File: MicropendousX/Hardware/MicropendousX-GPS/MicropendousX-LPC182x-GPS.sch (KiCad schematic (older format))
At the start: 0 parts

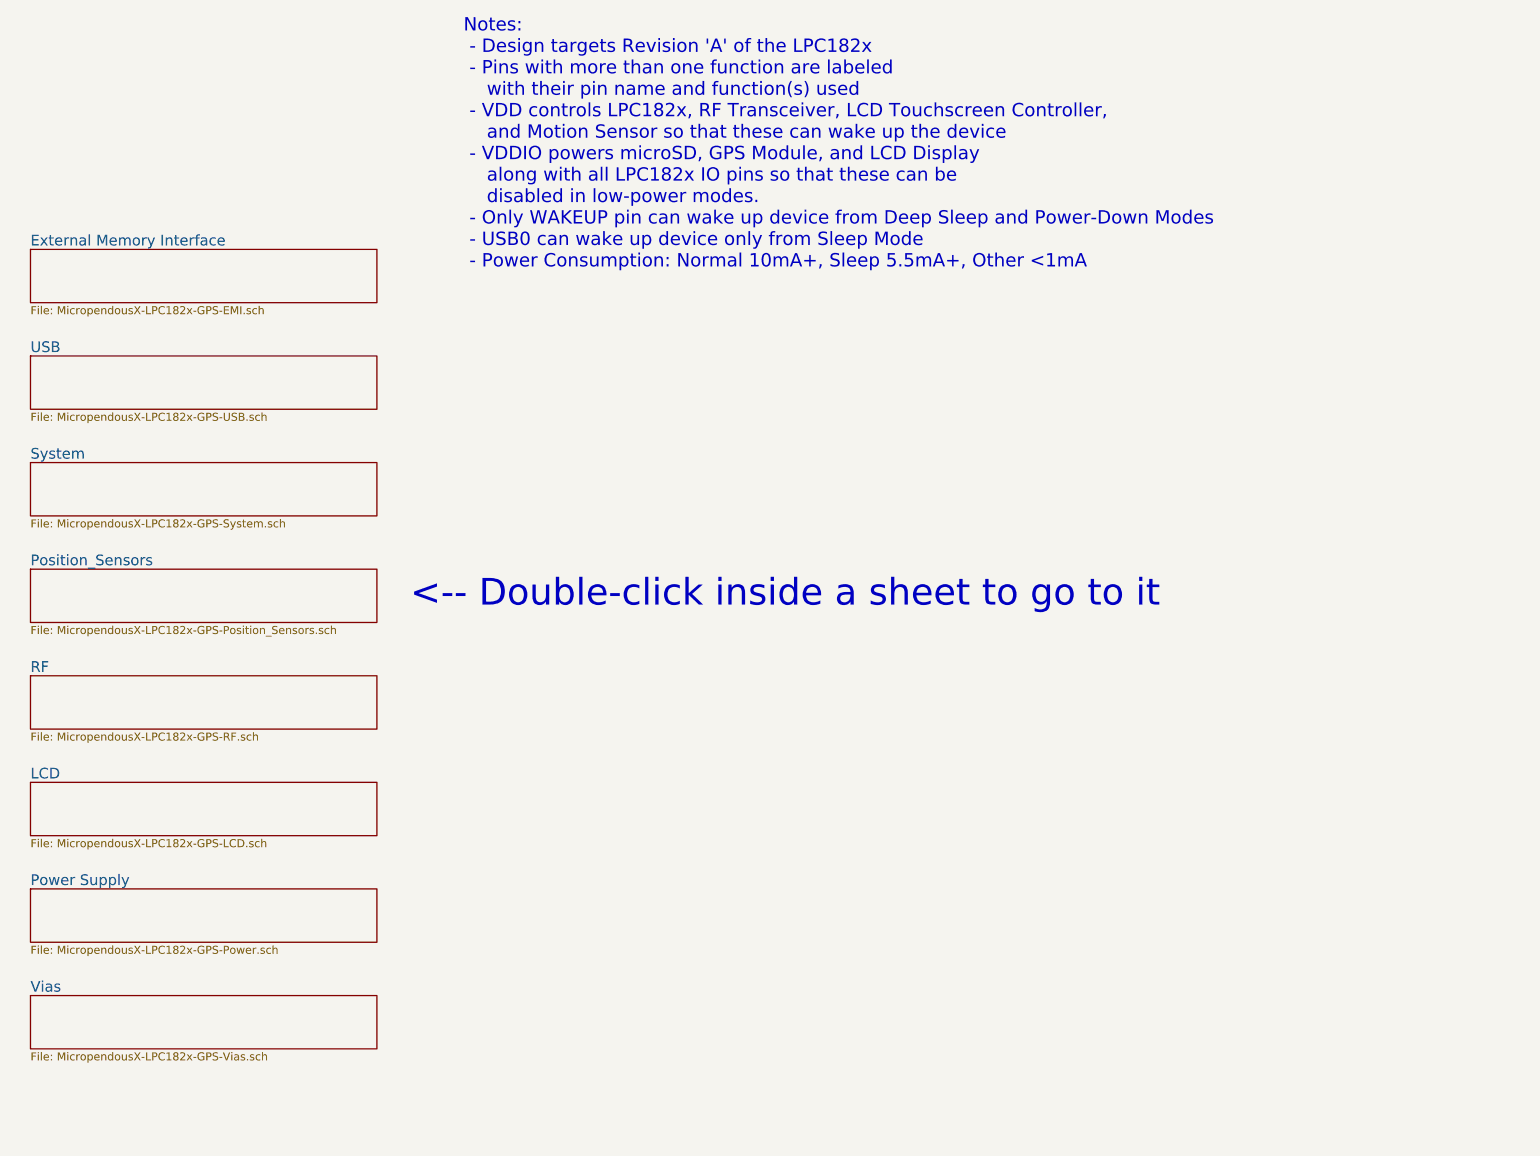
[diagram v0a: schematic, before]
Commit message: Updated MicropendousX-LPC182x-GPS design.  PCB routing almost complete.
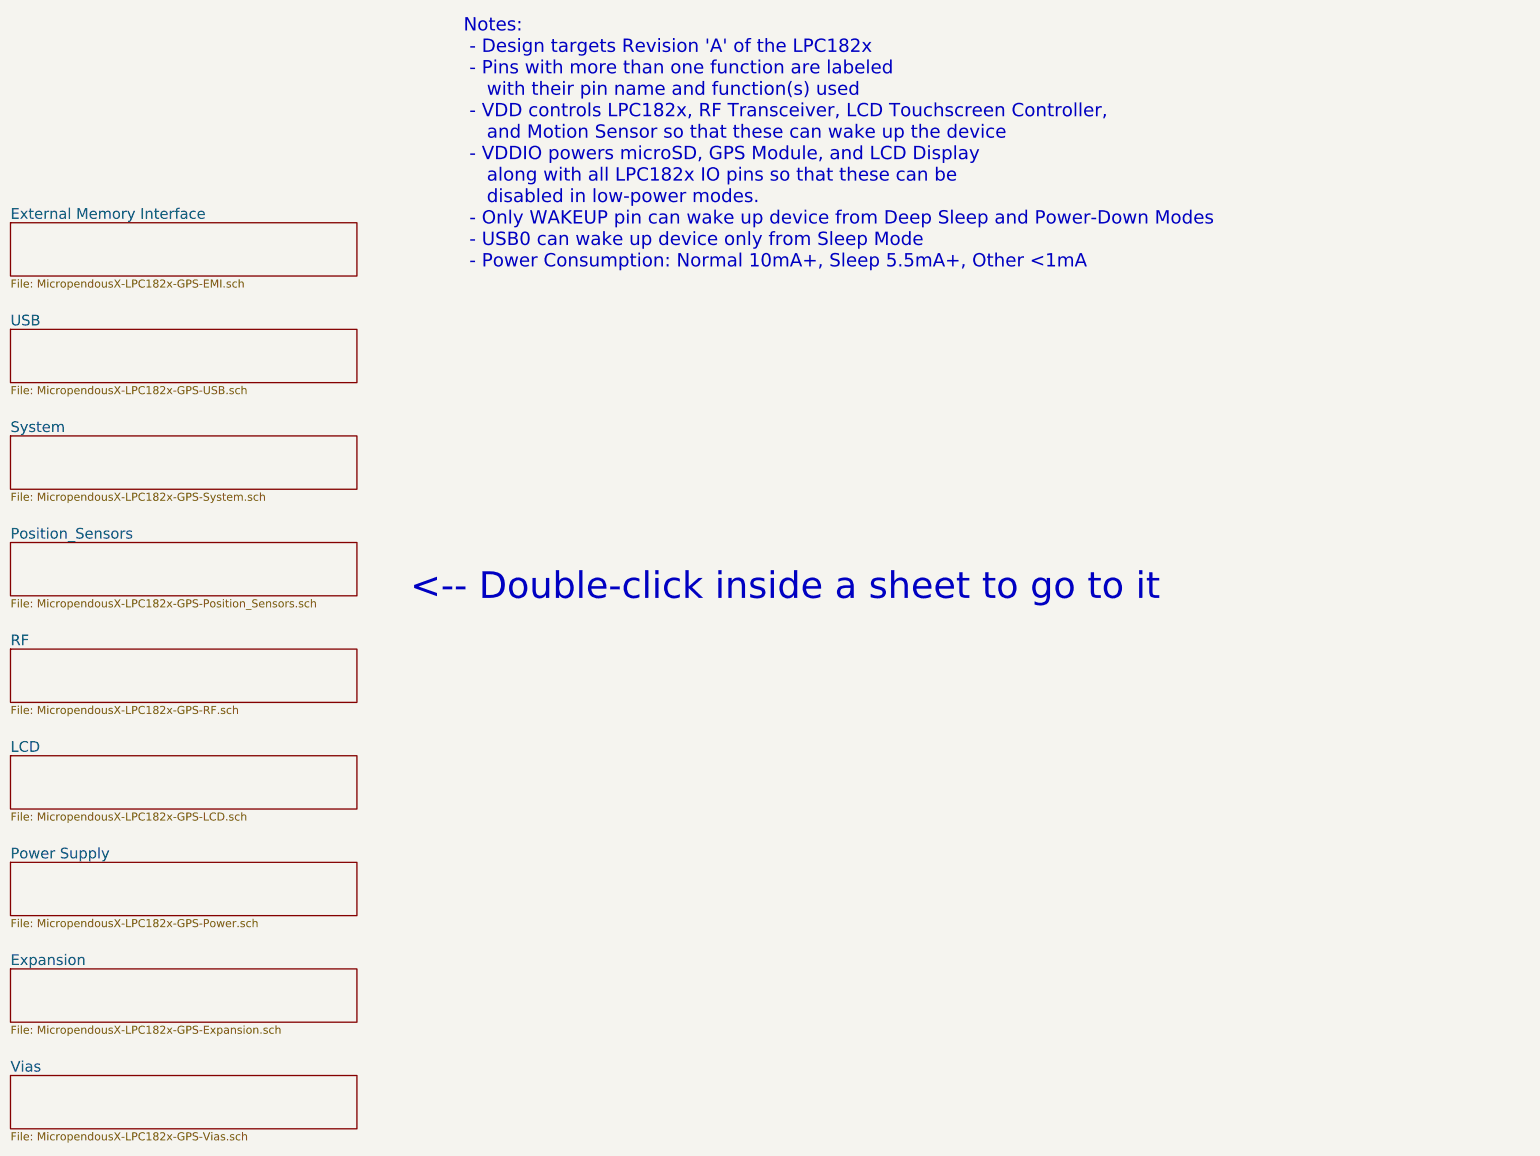
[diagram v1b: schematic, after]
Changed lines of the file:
@@
-EESchema Schematic File Version 2  date 5/31/2012 10:34:44 PM
+EESchema Schematic File Version 2  date 6/8/2012 3:21:19 PM
 LIBS:power
 LIBS:device
@@
 LIBS:contrib
 LIBS:valves
-LIBS:opendous
-LIBS:Opennect_Schematic_Symbols_Library
 LIBS:MicropendousX-LPC182x-GPS-cache
 EELAYER 25  0
@@
 $Descr A4 11700 8267
 encoding utf-8
-Sheet 1 9
+Sheet 1 10
 Title "MicropendousX-LPC182x-GPS"
-Date "1 jun 2012"
+Date "8 jun 2012"
 Rev "1.0"
 Comp "Opendous Inc."
@@
 $EndDescr
 $Sheet
-S 950  3400 2600 400
+S 800  7200 2600 400
+U 4FC9D4A0
+F0 "Vias" 80
+F1 "MicropendousX-LPC182x-GPS-Vias.sch" 60
+$EndSheet
+$Sheet
+S 800  3200 2600 400
 U 4FBDF1D6
 F0 "Position_Sensors" 80
@@
 $EndSheet
 $Sheet
-S 950  5000 2600 400
+S 800  4800 2600 400
 U 4FBDC8F3
 F0 "LCD" 80
@@
 $EndSheet
 $Sheet
-S 950  4200 2600 400
+S 800  4000 2600 400
 U 4FBDC8B6
 F0 "RF" 80
 F1 "MicropendousX-LPC182x-GPS-RF.sch" 60
 $EndSheet
-Text Notes 3800 3700 0    200  ~ 0
+Text Notes 3800 3650 0    200  ~ 0
 <-- Double-click inside a sheet to go to it
 Text Notes 4200 1150 0    100  ~ 0
 Notes:\n - Design targets Revision 'A' of the LPC182x\n - Pins with more than one function are labeled\n    with their pin name and function(s) used\n - VDD controls LPC182x, RF Transceiver, LCD Touchscreen Controller,\n    and Motion Sensor so that these can wake up the device\n - VDDIO powers microSD, GPS Module, and LCD Display\n    along with all LPC182x IO pins so that these can be\n    disabled in low-power modes.\n - Only WAKEUP pin can wake up device from Deep Sleep and Power-Down Modes\n - USB0 can wake up device only from Sleep Mode\n - Power Consumption: Normal 10mA+, Sleep 5.5mA+, Other <1mA
 $Sheet
-S 950  1000 2600 400
+S 800  800  2600 400
 U 4E1DDD2A
 F0 "External Memory Interface" 80
@@
 $EndSheet
 $Sheet
-S 950  1800 2600 400
+S 800  1600 2600 400
 U 4E1DDD6A
 F0 "USB" 80
@@
 $EndSheet
 $Sheet
-S 950  2600 2600 400
+S 800  2400 2600 400
 U 4E1DDD7A
 F0 "System" 80
@@
 $EndSheet
 $Sheet
-S 950  5800 2600 400
+S 800  5600 2600 400
 U 4E1DDB8A
 F0 "Power Supply" 80
@@
 $EndSheet
 $Sheet
-S 950  6600 2600 400
+S 800  6400 2600 400
 U 4E1DDDAA
-F0 "Vias" 80
-F1 "MicropendousX-LPC182x-GPS-Vias.sch" 60
+F0 "Expansion" 80
+F1 "MicropendousX-LPC182x-GPS-Expansion.sch" 60
 $EndSheet
 $EndSCHEMATC
